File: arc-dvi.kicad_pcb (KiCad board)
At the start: 4 copper layers, 100 x 77 mm, 143 parts, among them J1 Connector_50pin_FFC, J2 5V_IN, J3 SWD, J4 BOOT, J5 USB_B_Micro, J6 PWR_USB, J7 Misc, J8 HDMI_A, Q1 Q_NPN_BCE, U1 W25Q32JVSS, U2 RP2040, U3 ICE40HX4K-TQ144, U4 ADV7513BSWZ, U5 LT1963AxST-3.3, U6 TLV70012_SOT23-5, U7 TLV70018_SOT23-5, Y1 12M 18pF

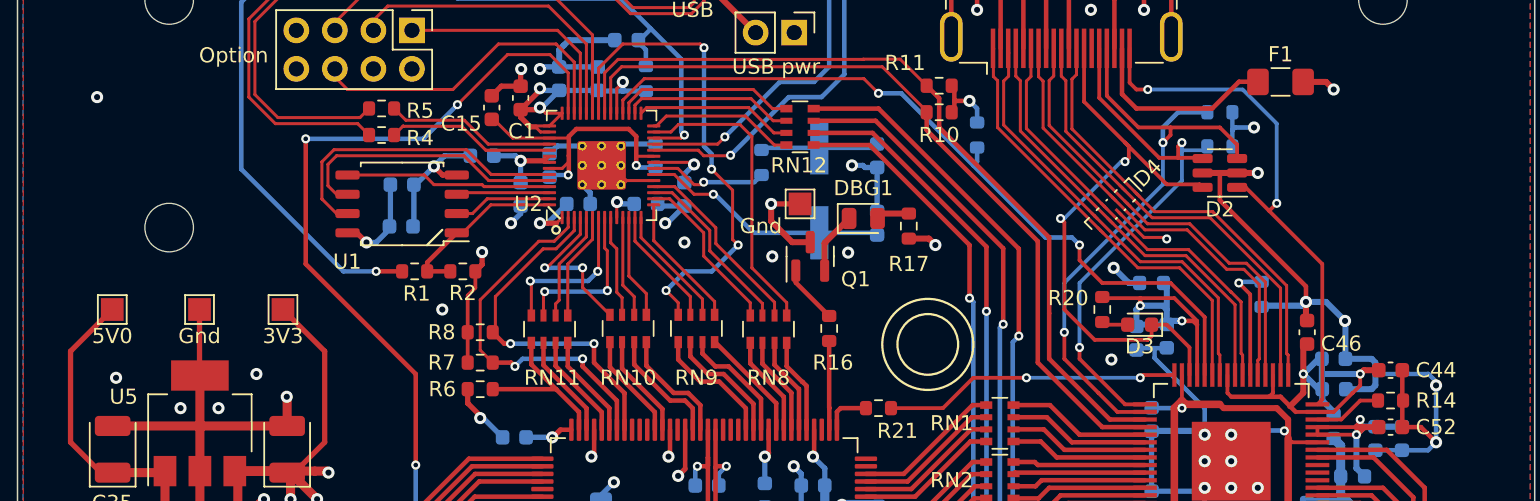
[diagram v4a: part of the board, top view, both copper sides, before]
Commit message: Moved Gnd TP, added decoration
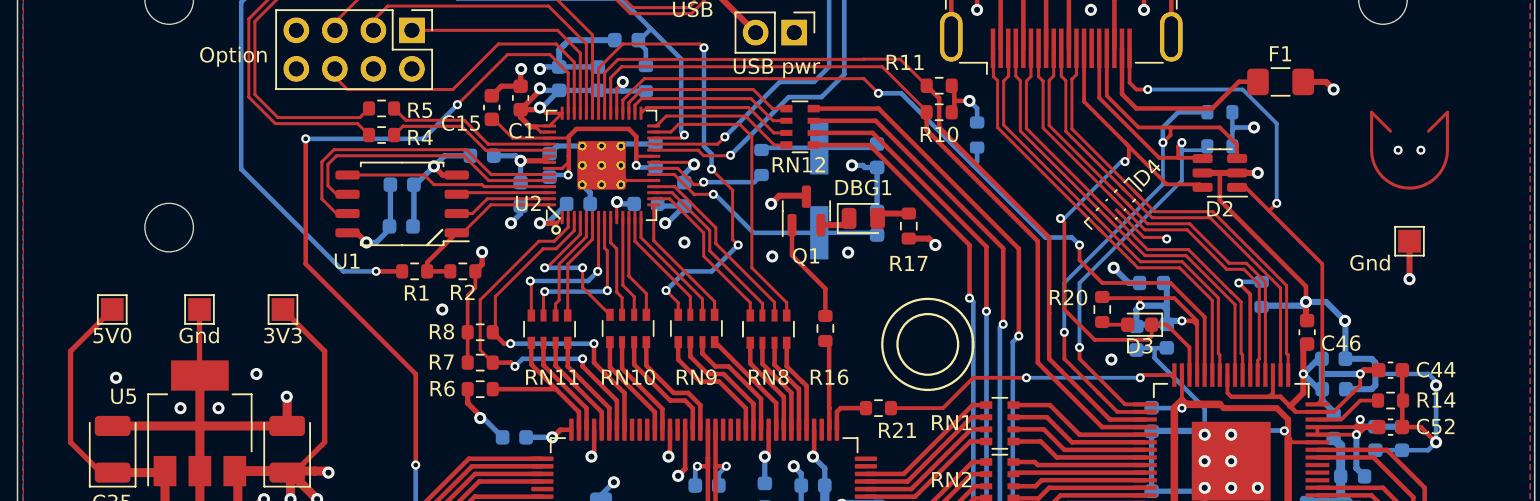
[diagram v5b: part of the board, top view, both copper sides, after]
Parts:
- moved TP21 40.2 mm to (141.8, 73.0)
- moved Q1 3.01 mm to (102.0, 71.0)
- moved R16 0.25 mm to (103.2, 78.8)
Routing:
- net Net-(Q1-Pad1): track 3.90 -> 6.90 mm
- net Net-(D1-Pad1): track 4.11 -> 2.04 mm
- net GND: track 964.2 -> 963.1 mm, vias 82 -> 84
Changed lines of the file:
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@@
   )
   (footprint "Resistor_SMD:R_0603_1608Metric" (layer "F.Cu")
-    (at 103.5 78.75 90)
+    (at 103.25 78.75 90)
     (descr "Resistor SMD 0603 (1608 Metric), square (rectangular) end terminal, IPC_7351 nominal, (Body size source: IPC-SM-782 page 72, https://www.pcb-3d.com/wordpress/wp-content/uploads/ipc-sm-782a_amendment_1_and_2.pdf), generated with kicad-footprint-generator")
     (tags "resistor")
@@
     (property "Sheetname" "FPGA")
     (attr smd)
-    (fp_text reference "R16" (at -2.25 0.25 180) (layer "F.SilkS")
+    (fp_text reference "R16" (at -3.25 0.25 180) (layer "F.SilkS")
       (effects (font (size 1 1) (thickness 0.15)))
     )
@@
   )
   (footprint "Package_TO_SOT_SMD:SOT-23" (layer "F.Cu")
-    (at 102.25 74 90)
+    (at 102 71 90)
     (descr "SOT, 3 Pin (https://www.jedec.org/system/files/docs/to-236h.pdf variant AB), generated with kicad-footprint-generator ipc_gullwing_generator.py")
     (tags "SOT TO_SOT_SMD")
@@
     (property "Sheetname" "FPGA")
     (attr smd)
-    (fp_text reference "Q1" (at -1.5 3 180) (layer "F.SilkS")
+    (fp_text reference "Q1" (at -3 0 180) (layer "F.SilkS")
       (effects (font (size 1 1) (thickness 0.15)))
     )
@@
   )
   (footprint "TestPoint:TestPoint_Pad_1.5x1.5mm" (layer "F.Cu")
-    (at 101.58 70.54)
+    (at 141.75 73)
     (descr "SMD rectangular pad as test Point, square 1.5mm side length")
     (tags "test point SMD pad rectangle square")
@@
     )
   )
+  (gr_line (start 140.5 65.75) (end 139.25 64.5) (layer "F.Cu") (width 0.2))
+  (gr_line (start 144.25 64.5) (end 143 65.75) (layer "F.Cu") (width 0.2))
+  (gr_line (start 139.25 64.5) (end 139.25 67) (layer "F.Cu") (width 0.2))
+  (gr_line (start 144.25 67) (end 144.25 64.5) (layer "F.Cu") (width 0.2))
+  (gr_arc (start 144.25 67) (mid 141.75 69.5) (end 139.25 67) (layer "F.Cu") (width 0.2))
   (gr_circle (center 110 79.8) (end 113 79.8) (layer "B.SilkS") (width 0.15) (fill none))
   (gr_circle (center 136.5 92) (end 136.5 91.75) (layer "F.SilkS") (width 0.15) (fill none))
@@
   (segment (start 134.925 75.975) (end 134.925 77) (width 0.3) (layer "F.Cu") (net 2))
   (segment (start 104.7 120.25053) (end 104.77702 120.32755) (width 0.4) (layer "F.Cu") (net 2))
-  (segment (start 102.25 73.0625) (end 101.0625 73.0625) (width 0.4) (layer "F.Cu") (net 2))
   (segment (start 87.35 123.4) (end 83.35 123.4) (width 0.4) (layer "F.Cu") (net 2))
   (segment (start 78.955 68.635) (end 78.0205 68.635) (width 0.35) (layer "F.Cu") (net 2))
@@
   (segment (start 98.01 104.955) (end 98.625 104.34) (width 0.3) (layer "F.Cu") (net 2))
   (segment (start 104.63 98.335) (end 103.995 98.335) (width 0.35) (layer "F.Cu") (net 2))
-  (segment (start 101.0625 73.0625) (end 99.675 71.675) (width 0.4) (layer "F.Cu") (net 2))
   (segment (start 119.25 56.75) (end 118 56.75) (width 0.3) (layer "F.Cu") (net 2))
   (segment (start 99.86053 120.86053) (end 99.455 120.455) (width 0.4) (layer "F.Cu") (net 2))
   (segment (start 62.025 81.85) (end 62.025 85.325) (width 0.6) (layer "F.Cu") (net 2))
   (segment (start 122.3 60.285) (end 122.3 57.05) (width 0.3) (layer "F.Cu") (net 2))
+  (segment (start 102 70.0625) (end 101.9375 70) (width 0.4) (layer "F.Cu") (net 2))
   (segment (start 122.3 57.05) (end 122 56.75) (width 0.3) (layer "F.Cu") (net 2))
   (segment (start 134.75 98) (end 134.75 96.8) (width 0.3) (layer "F.Cu") (net 2))
@@
   (segment (start 116.3 56.95) (end 116.5 56.75) (width 0.3) (layer "F.Cu") (net 2))
   (segment (start 62.175 85.175) (end 56.275 85.175) (width 0.6) (layer "F.Cu") (net 2))
-  (segment (start 99.675 71.675) (end 99.675 70.54) (width 0.4) (layer "F.Cu") (net 2))
   (segment (start 116.5 56.75) (end 115 56.75) (width 0.3) (layer "F.Cu") (net 2))
   (segment (start 131.645 114.5) (end 132.28 113.865) (width 0.35) (layer "F.Cu") (net 2))
@@
   (segment (start 95.75 52.7) (end 93.45 52.7) (width 0.4) (layer "F.Cu") (net 2))
   (segment (start 134.925 78.15) (end 135 78.225) (width 0.4) (layer "F.Cu") (net 2))
+  (segment (start 101.9375 70) (end 100.215 70) (width 0.4) (layer "F.Cu") (net 2))
   (segment (start 142.5 85.25) (end 143.5 86.25) (width 0.3) (layer "F.Cu") (net 2))
   (segment (start 112.69 122.62553) (end 111.7875 121.72303) (width 0.4) (layer "F.Cu") (net 2))
@@
   (segment (start 93.45 52.7) (end 90.85 52.7) (width 0.35) (layer "F.Cu") (net 2))
   (segment (start 104.8525 117.86303) (end 104.7 118.01553) (width 0.4) (layer "F.Cu") (net 2))
+  (segment (start 100.215 70) (end 99.675 70.54) (width 0.4) (layer "F.Cu") (net 2))
   (segment (start 128.1125 68.5) (end 129.25 68.5) (width 0.4) (layer "F.Cu") (net 2))
   (segment (start 91.9375 69) (end 90.05 69) (width 0.2) (layer "F.Cu") (net 2))
@@
   (segment (start 79.25 123.25) (end 79.4 123.4) (width 0.25) (layer "F.Cu") (net 2))
   (segment (start 115 56.75) (end 114.8 56.95) (width 0.3) (layer "F.Cu") (net 2))
-  (segment (start 99.675 70.54) (end 101.58 70.54) (width 0.35) (layer "F.Cu") (net 2))
   (segment (start 126.565 120.215) (end 122.965 120.215) (width 0.35) (layer "F.Cu") (net 2))
   (segment (start 90.75 120.15) (end 90.75 123.3) (width 0.25) (layer "F.Cu") (net 2))
@@
   (segment (start 89.15 123.4) (end 87.35 123.4) (width 0.4) (layer "F.Cu") (net 2))
   (segment (start 75.4 123.4) (end 75.9 123.4) (width 0.25) (layer "F.Cu") (net 2))
+  (segment (start 141.75 73) (end 141.75 75.5) (width 0.4) (layer "F.Cu") (net 2))
   (segment (start 83.25 120.15) (end 83.25 123.3) (width 0.25) (layer "F.Cu") (net 2))
   (segment (start 67.775 85.175) (end 67.775 83.275) (width 0.6) (layer "F.Cu") (net 2))
@@
   (via (at 99.675 70.54) (size 0.8) (drill 0.4) (layers "F.Cu" "B.Cu") (free) (net 2))
   (via (at 80.5 84.655) (size 0.8) (drill 0.4) (layers "F.Cu" "B.Cu") (net 2))
-  (via (at 55.25 63.5) (size 0.8) (drill 0.4) (layers "F.Cu" "B.Cu") (net 2))
+  (via (at 141 67) (size 0.6) (drill 0.3) (layers "F.Cu" "B.Cu") (net 2))
   (via (at 125.75 72.8505) (size 0.6) (drill 0.3) (layers "F.Cu" "B.Cu") (net 2))
   (via (at 89 122.5) (size 0.8) (drill 0.4) (layers "F.Cu" "B.Cu") (net 2))
@@
   (via (at 98.625 104.34) (size 0.8) (drill 0.4) (layers "F.Cu" "B.Cu") (net 2))
   (via (at 87.83 87.195) (size 0.8) (drill 0.4) (layers "F.Cu" "B.Cu") (net 2))
+  (via (at 142.5 67) (size 0.6) (drill 0.3) (layers "F.Cu" "B.Cu") (net 2))
   (via (at 110.75 118.5) (size 0.8) (drill 0.4) (layers "F.Cu" "B.Cu") (net 2))
   (via (at 112.75 122.62553) (size 0.8) (drill 0.4) (layers "F.Cu" "B.Cu") (net 2))
@@
   (via (at 66.25 93) (size 0.8) (drill 0.4) (layers "F.Cu" "B.Cu") (net 2))
   (via (at 107 116.25) (size 0.8) (drill 0.4) (layers "F.Cu" "B.Cu") (free) (net 2))
+  (via (at 141.75 75.5) (size 0.8) (drill 0.4) (layers "F.Cu" "B.Cu") (net 2))
   (via (at 93.96 73.08) (size 0.8) (drill 0.4) (layers "F.Cu" "B.Cu") (free) (net 2))
   (via (at 103.705 98.625) (size 0.8) (drill 0.4) (layers "F.Cu" "B.Cu") (net 2))
@@
   (segment (start 102.51 108.860678) (end 104.149322 110.5) (width 0.3) (layer "F.Cu") (net 189))
   (segment (start 104.149322 110.5) (end 107.5 110.5) (width 0.3) (layer "F.Cu") (net 189))
-  (segment (start 103.2 73.1125) (end 104.8125 71.5) (width 0.4) (layer "F.Cu") (net 190))
-  (segment (start 103.2 74.9375) (end 103.2 73.1125) (width 0.4) (layer "F.Cu") (net 190))
+  (segment (start 102.95 71.9375) (end 104.375 71.9375) (width 0.4) (layer "F.Cu") (net 190))
+  (segment (start 104.375 71.9375) (end 104.8125 71.5) (width 0.4) (layer "F.Cu") (net 190))
   (segment (start 107.0125 71.175) (end 106.6875 71.5) (width 0.4) (layer "F.Cu") (net 191))
   (segment (start 108.75 71.175) (end 107.0125 71.175) (width 0.4) (layer "F.Cu") (net 191))
-  (segment (start 101.3 74.9375) (end 101.3 75.725) (width 0.3) (layer "F.Cu") (net 192))
-  (segment (start 101.3 75.725) (end 103.5 77.925) (width 0.3) (layer "F.Cu") (net 192))
+  (segment (start 101.05 71.9375) (end 101.05 73.925) (width 0.3) (layer "F.Cu") (net 192))
+  (segment (start 103.25 76.125) (end 103.25 77.925) (width 0.3) (layer "F.Cu") (net 192))
+  (segment (start 101.05 73.925) (end 103.25 76.125) (width 0.3) (layer "F.Cu") (net 192))
   (segment (start 103.51 85.4225) (end 103.51 83.99) (width 0.3) (layer "F.Cu") (net 193))
-  (segment (start 103.5 83.98) (end 103.5 79.575) (width 0.3) (layer "F.Cu") (net 193))
+  (segment (start 103.5 83.98) (end 103.5 79.825) (width 0.3) (layer "F.Cu") (net 193))
   (segment (start 103.51 83.99) (end 103.5 83.98) (width 0.3) (layer "F.Cu") (net 193))
+  (segment (start 103.5 79.825) (end 103.25 79.575) (width 0.3) (layer "F.Cu") (net 193))
   (segment (start 95.9 55.55) (end 95.9 56.495) (width 0.4) (layer "F.Cu") (net 196))
   (segment (start 95.9 56.495) (end 98.655 59.25) (width 0.4) (layer "F.Cu") (net 196))
